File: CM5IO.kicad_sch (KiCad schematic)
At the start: 14 parts, among them J11 USB_C_Receptacle_USB2.0, J4 ATX-24, Q1 MMBT7002K

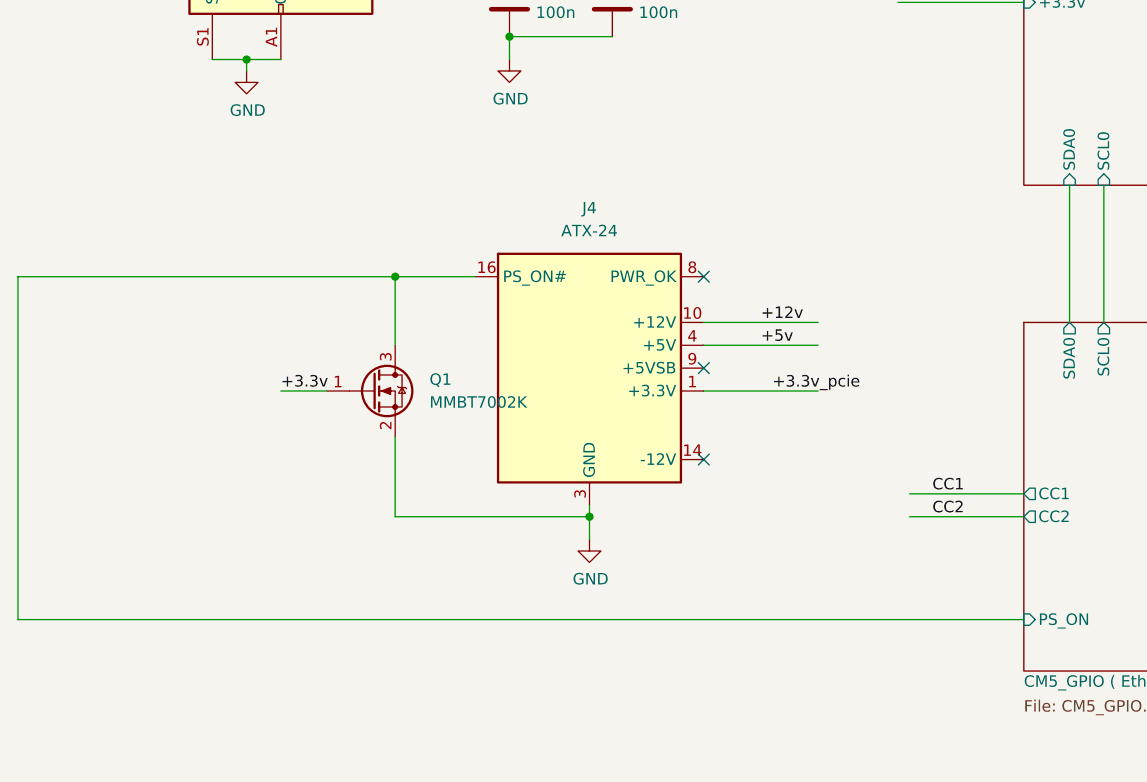
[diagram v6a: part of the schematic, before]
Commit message: add ideal diode to ATX
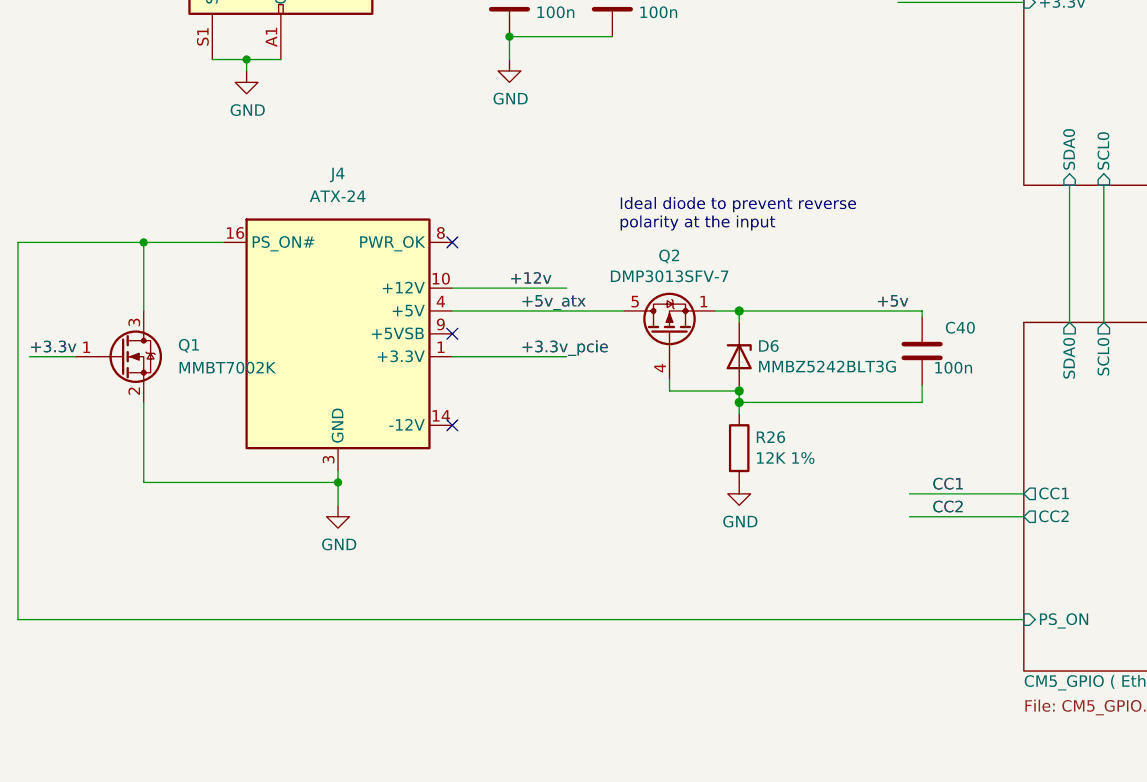
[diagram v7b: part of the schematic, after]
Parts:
- added C40: 100n, Capacitor_SMD:C_0402_1005Metric, symbol Device:C
- added D6: MMBZ5242BLT3G, Diode_SMD:D_SOT-23_ANK, symbol Diode:BZX84Cxx
- added Q2: DMP3013SFV-7, Package_SON:Diodes_PowerDI3333-8, symbol Transistor_FET:DMP3013SFV
- added R26: 12K 1%, Resistor_SMD:R_0402_1005Metric, symbol Device:R
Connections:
- net +5v: now also C40.1, D6.1 (K), Q2.1 (S), Q2.2 (S), Q2.3 (S); no longer J4.21 (+5V), J4.22 (+5V), J4.23 (+5V), J4.4 (+5V), J4.6 (+5V)
- net GND: now also R26.2
- new net: C40.2, D6.2 (A), Q2.4 (G), R26.1
- new net +5v_atx: J4.21 (+5V), J4.22 (+5V), J4.23 (+5V), J4.4 (+5V), J4.6 (+5V), Q2.5 (D)
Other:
- note added: "Ideal diode to prevent reverse polarity at the input"
- moved on the sheet: J4, Q1

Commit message: more aisler changes
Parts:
- removed D6: MMBZ5242BLT3G, Diode_SMD:D_SOT-23_ANK, symbol Diode:BZX84Cxx
- added D7: D_Zener_Dual_CommonCathode_AAK_Split, Package_TO_SOT_SMD:SOT-23, symbol Device:D_Zener_Dual_CommonCathode_AAK_Split
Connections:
- net +5v: now also D7.3 (K)
- net at C40.2, Q2.4 (G), R26.1: now also D7.1 (A)
